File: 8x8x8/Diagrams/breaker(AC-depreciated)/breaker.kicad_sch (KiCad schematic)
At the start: 1 part

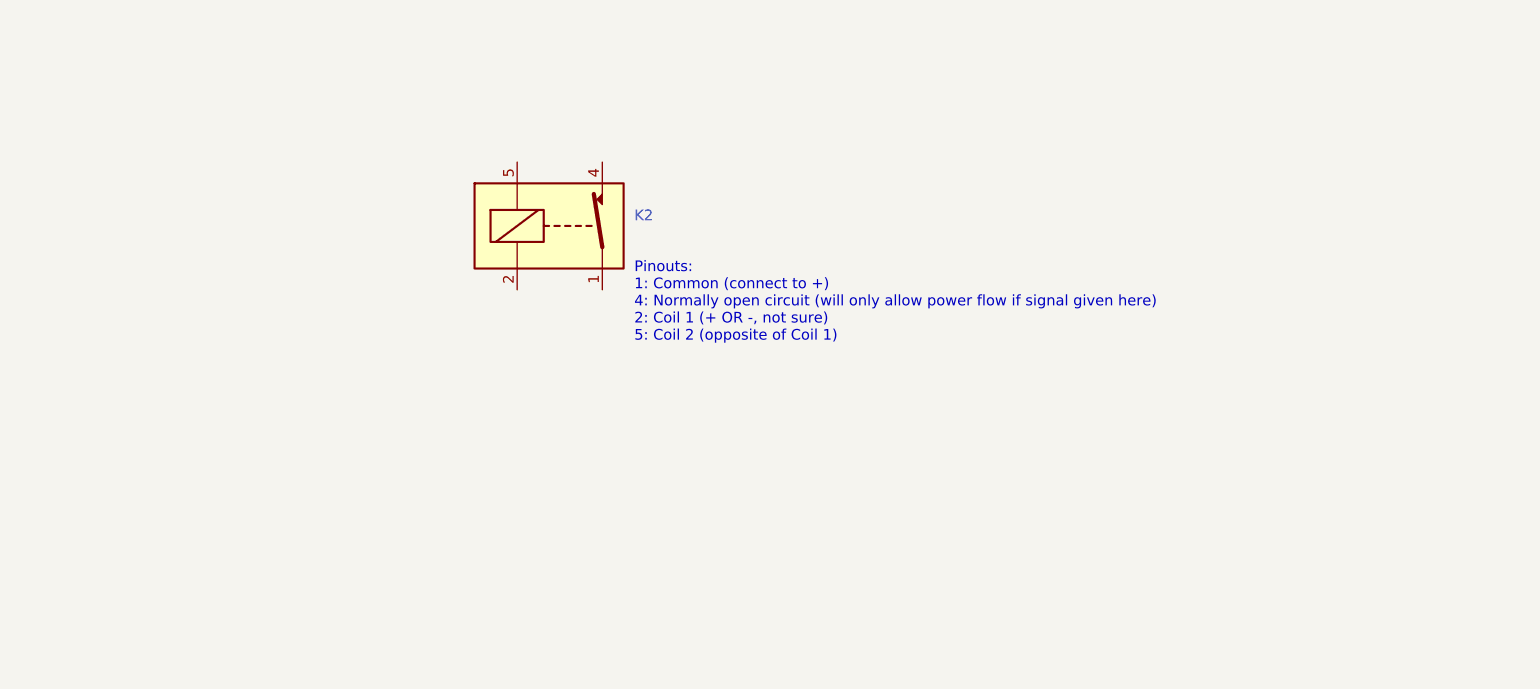
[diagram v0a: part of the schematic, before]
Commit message: Add sample AC switch. Start DC transistor switch.
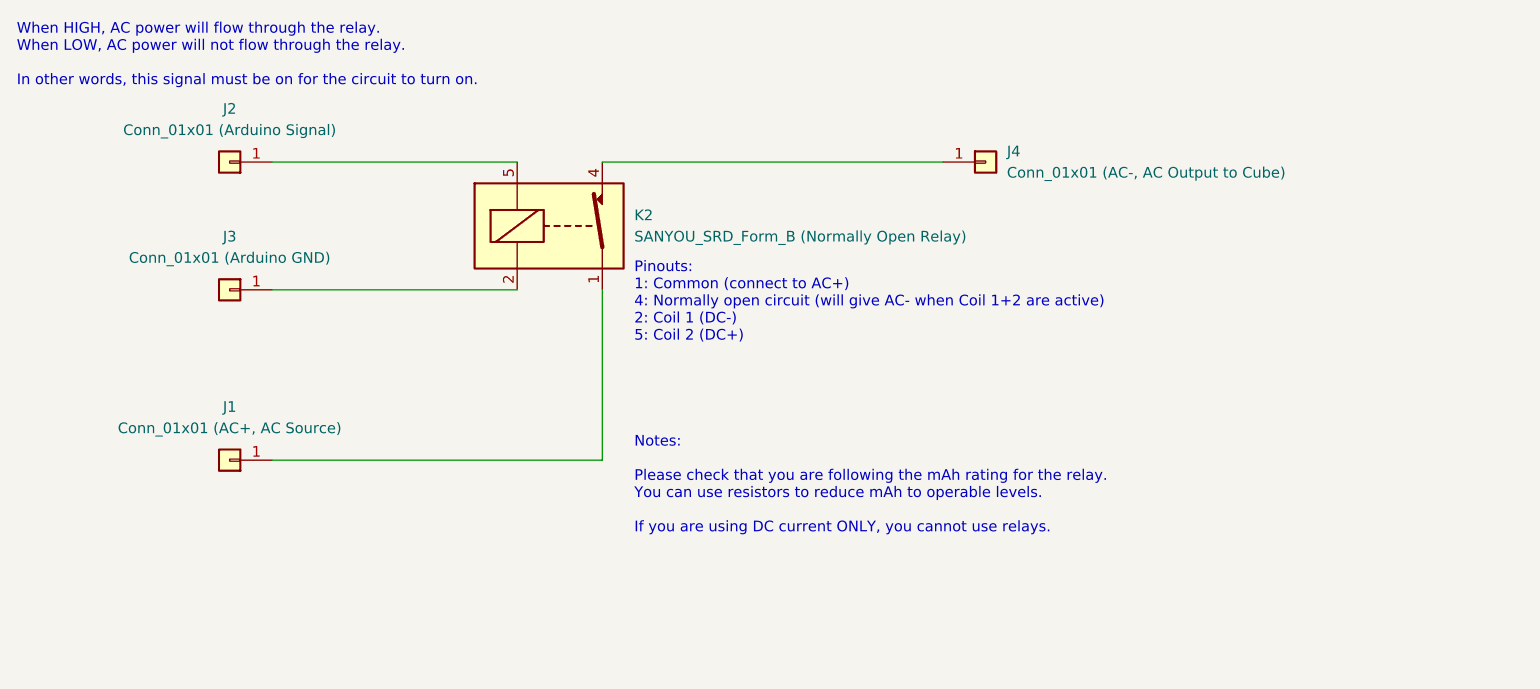
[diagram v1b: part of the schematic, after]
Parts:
- added J1: Conn_01x01 (AC+, AC Source), symbol Connector_Generic:Conn_01x01
- added J2: Conn_01x01 (Arduino Signal), symbol Connector_Generic:Conn_01x01
- added J3: Conn_01x01 (Arduino GND), symbol Connector_Generic:Conn_01x01
- added J4: Conn_01x01 (AC-, AC Output to Cube), symbol Connector_Generic:Conn_01x01
- K2: value (none) -> SANYOU_SRD_Form_B (Normally Open Relay)
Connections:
- net at K2.1: now also J1.1 (Pin_1)
- net at K2.2: now also J3.1 (Pin_1)
- net at K2.4: now also J4.1 (Pin_1)
- net at K2.5: now also J2.1 (Pin_1)
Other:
- note added: "Notes: Please check that you are following the mAh rating for the relay. You can use resistors to reduce mAh to operable levels. If you are using DC current ONLY, you cannot use relays."
- note added: "Pinouts: 1: Common (connect to AC+) 4: Normally open circuit (will give AC- when Coil 1+2 are active) 2: Coil 1 (DC-) 5: Coil 2 (DC+)"
- note added: "When HIGH, AC power will flow through the relay. When LOW, AC power will not flow through the relay. In other words, this signal must be on for the circuit to turn on."
- note removed: "Pinouts: 1: Common (connect to +) 4: Normally open circuit (will only allow power flow if signal given here) 2: Coil 1 (+ OR -, not sure) 5: Coil 2 (opposite of Coil 1)"
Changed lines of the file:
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@@
 (kicad_sch (version 20211123) (generator eeschema)
   (paper "A4")
+  (wire (pts (xy 105.41 104.14) (xy 105.41 83.82))
+    (stroke (width 0) (type default) (color 0 0 0 0))
+  )
+  (wire (pts (xy 105.41 68.58) (xy 146.05 68.58))
+    (stroke (width 0) (type default) (color 0 0 0 0))
+  )
+  (wire (pts (xy 66.04 68.58) (xy 95.25 68.58))
+    (stroke (width 0) (type default) (color 0 0 0 0))
+  )
+  (wire (pts (xy 66.04 83.82) (xy 95.25 83.82))
+    (stroke (width 0) (type default) (color 0 0 0 0))
+  )
+  (wire (pts (xy 66.04 104.14) (xy 105.41 104.14))
+    (stroke (width 0) (type default) (color 0 0 0 0))
+  )
   (text "June 30 2022" (at 207.01 194.31 0)
     (effects (font (size 1.27 1.27)) (justify left bottom))
@@
     (effects (font (size 2.8 2.8)) (justify left bottom))
   )
+  (text "When HIGH, AC power will flow through the relay.\nWhen LOW, AC power will not flow through the relay.\n\nIn other words, this signal must be on for the circuit to turn on."
+    (at 35.56 59.69 0)
+    (effects (font (size 1.27 1.27)) (justify left bottom))
+  )
   (text "0.1.0\n" (at 269.24 194.31 0)
     (effects (font (size 1.27 1.27)) (justify left bottom))
   )
-  (text "Pinouts:\n1: Common (connect to +)\n4: Normally open circuit (will only allow power flow if signal given here)\n2: Coil 1 (+ OR -, not sure)\n5: Coil 2 (opposite of Coil 1)\n"
+  (text "Pinouts:\n1: Common (connect to AC+)\n4: Normally open circuit (will give AC- when Coil 1+2 are active)\n2: Coil 1 (DC-)\n5: Coil 2 (DC+)\n"
     (at 109.22 90.17 0)
     (effects (font (size 1.27 1.27)) (justify left bottom))
+  )
+  (text "Notes:\n\nPlease check that you are following the mAh rating for the relay. \nYou can use resistors to reduce mAh to operable levels.\n\nIf you are using DC current ONLY, you cannot use relays."
+    (at 109.22 113.03 0)
+    (effects (font (size 1.27 1.27)) (justify left bottom))
+  )
+  (symbol (lib_id "Connector_Generic:Conn_01x01") (at 151.13 68.58 0) (unit 1)
+    (in_bom yes) (on_board yes) (fields_autoplaced)
+    (property "Reference" "J4" (id 0) (at 153.67 67.3099 0)
+      (effects (font (size 1.27 1.27)) (justify left))
+    )
+    (property "Value" "Conn_01x01 (AC-, AC Output to Cube)" (id 1) (at 153.67 69.8499 0)
+      (effects (font (size 1.27 1.27)) (justify left))
+    )
+    (property "Footprint" "" (id 2) (at 151.13 68.58 0)
+      (effects (font (size 1.27 1.27)) hide)
+    )
+    (property "Datasheet" "~" (id 3) (at 151.13 68.58 0)
+      (effects (font (size 1.27 1.27)) hide)
+    )
+    (pin "1")
+  )
+  (symbol (lib_id "Connector_Generic:Conn_01x01") (at 60.96 104.14 180) (unit 1)
+    (in_bom yes) (on_board yes) (fields_autoplaced)
+    (property "Reference" "J1" (id 0) (at 60.96 97.79 0))
+    (property "Value" "Conn_01x01 (AC+, AC Source)" (id 1) (at 60.96 100.33 0))
+    (property "Footprint" "" (id 2) (at 60.96 104.14 0)
+      (effects (font (size 1.27 1.27)) hide)
+    )
+    (property "Datasheet" "~" (id 3) (at 60.96 104.14 0)
+      (effects (font (size 1.27 1.27)) hide)
+    )
+    (pin "1")
   )
   (symbol (lib_id "Relay:SANYOU_SRD_Form_B") (at 100.33 76.2 0) (unit 1)
@@
       (effects (font (size 1.27 1.27)) (justify left))
     )
-    (property "Value" "" (id 1) (at 109.22 77.4699 0)
+    (property "Value" "SANYOU_SRD_Form_B (Normally Open Relay)" (id 1) (at 109.22 77.4699 0)
       (effects (font (size 1.27 1.27)) (justify left))
     )
@@
     (pin "5")
   )
+  (symbol (lib_id "Connector_Generic:Conn_01x01") (at 60.96 68.58 180) (unit 1)
+    (in_bom yes) (on_board yes) (fields_autoplaced)
+    (property "Reference" "J2" (id 0) (at 60.96 62.23 0))
+    (property "Value" "Conn_01x01 (Arduino Signal)" (id 1) (at 60.96 64.77 0))
+    (property "Footprint" "" (id 2) (at 60.96 68.58 0)
+      (effects (font (size 1.27 1.27)) hide)
+    )
+    (property "Datasheet" "~" (id 3) (at 60.96 68.58 0)
+      (effects (font (size 1.27 1.27)) hide)
+    )
+    (pin "1")
+  )
+  (symbol (lib_id "Connector_Generic:Conn_01x01") (at 60.96 83.82 0) (mirror y) (unit 1)
+    (in_bom yes) (on_board yes) (fields_autoplaced)
+    (property "Reference" "J3" (id 0) (at 60.96 77.47 0))
+    (property "Value" "Conn_01x01 (Arduino GND)" (id 1) (at 60.96 80.01 0))
+    (property "Footprint" "" (id 2) (at 60.96 83.82 0)
+      (effects (font (size 1.27 1.27)) hide)
+    )
+    (property "Datasheet" "~" (id 3) (at 60.96 83.82 0)
+      (effects (font (size 1.27 1.27)) hide)
+    )
+    (pin "1")
+  )
   (sheet_instances
     (path "/" (page "1"))
   )
   (symbol_instances
+    (path "/4107ae43-ef7b-4881-bf28-19412946e234"
+      (reference "J1") (unit 1) (value "Conn_01x01 (AC+, AC Source)") (footprint "")
+    )
+    (path "/883fdba5-f647-446e-8db4-99b5492ced0c"
+      (reference "J2") (unit 1) (value "Conn_01x01 (Arduino Signal)") (footprint "")
+    )
+    (path "/afe948da-6ab0-42e7-a1f3-2a759be377bf"
+      (reference "J3") (unit 1) (value "Conn_01x01 (Arduino GND)") (footprint "")
+    )
+    (path "/2afe99df-de6e-45f9-b645-bb8c3565d8b2"
+      (reference "J4") (unit 1) (value "Conn_01x01 (AC-, AC Output to Cube)") (footprint "")
+    )
     (path "/5d0be09d-133e-4cac-b0d8-fd336835cc6c"
       (reference "K2") (unit 1) (value "SANYOU_SRD_Form_B (Normally Open Relay)") (footprint "Relay_THT:Relay_SPST_SANYOU_SRD_Series_Form_B")
